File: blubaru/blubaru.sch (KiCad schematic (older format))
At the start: 24 parts, among them J1 TPA6112, J2 RN52_BREAKOUT

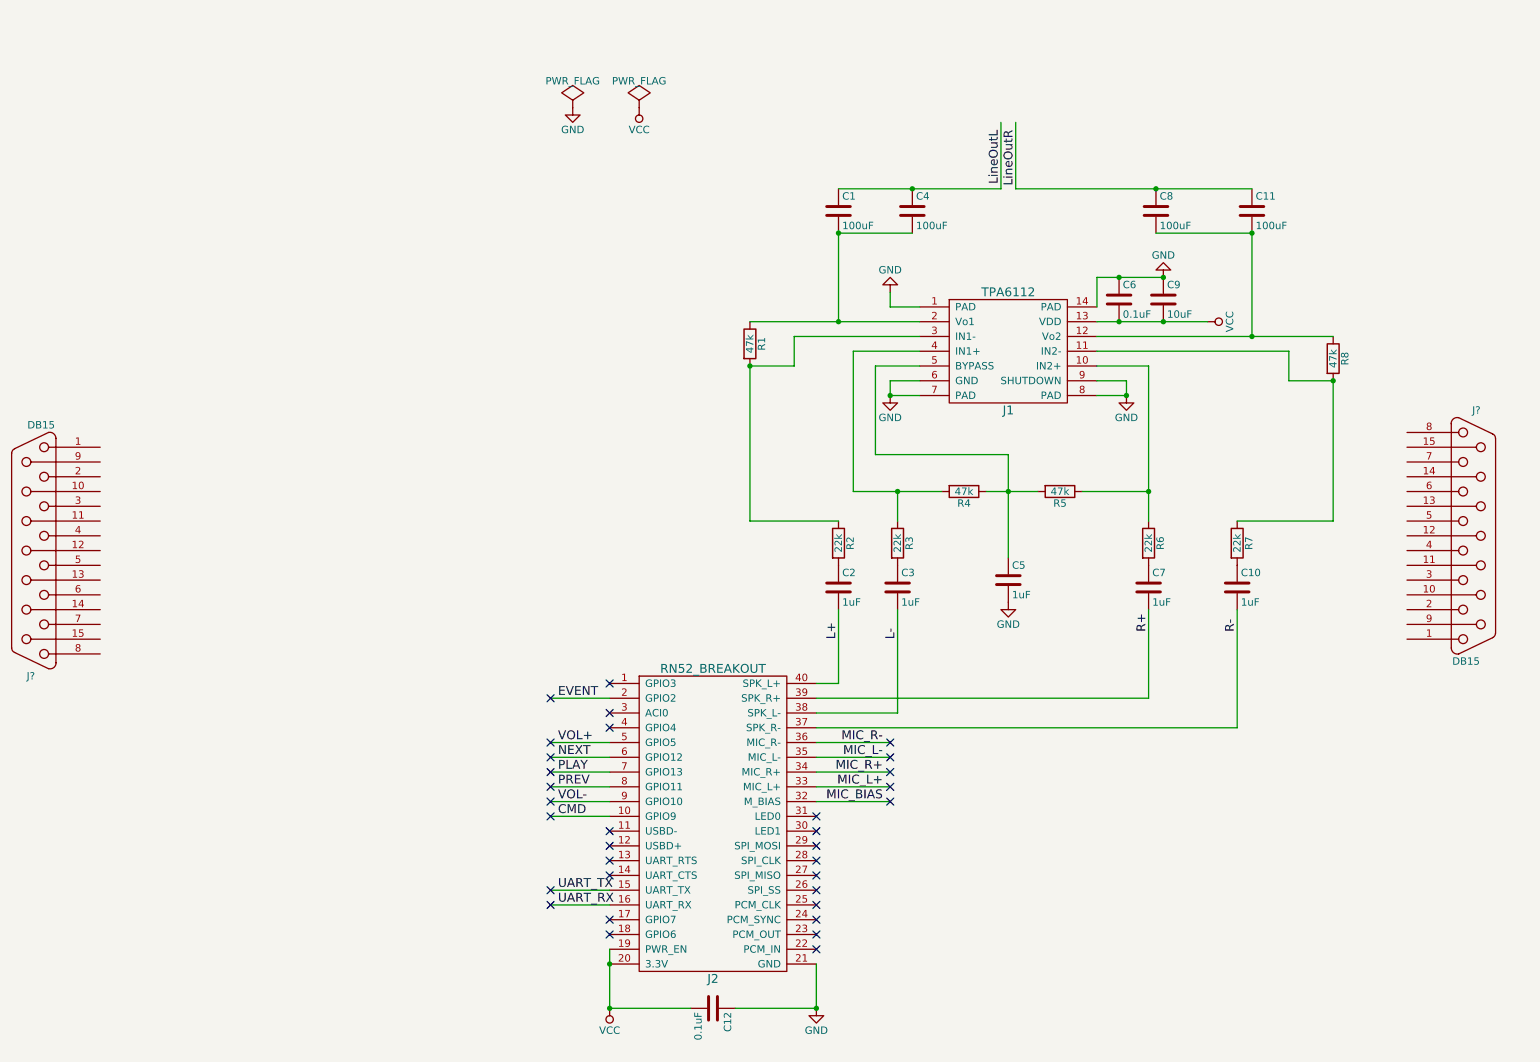
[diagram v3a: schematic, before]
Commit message: Add ProMicro board and DB15 labels
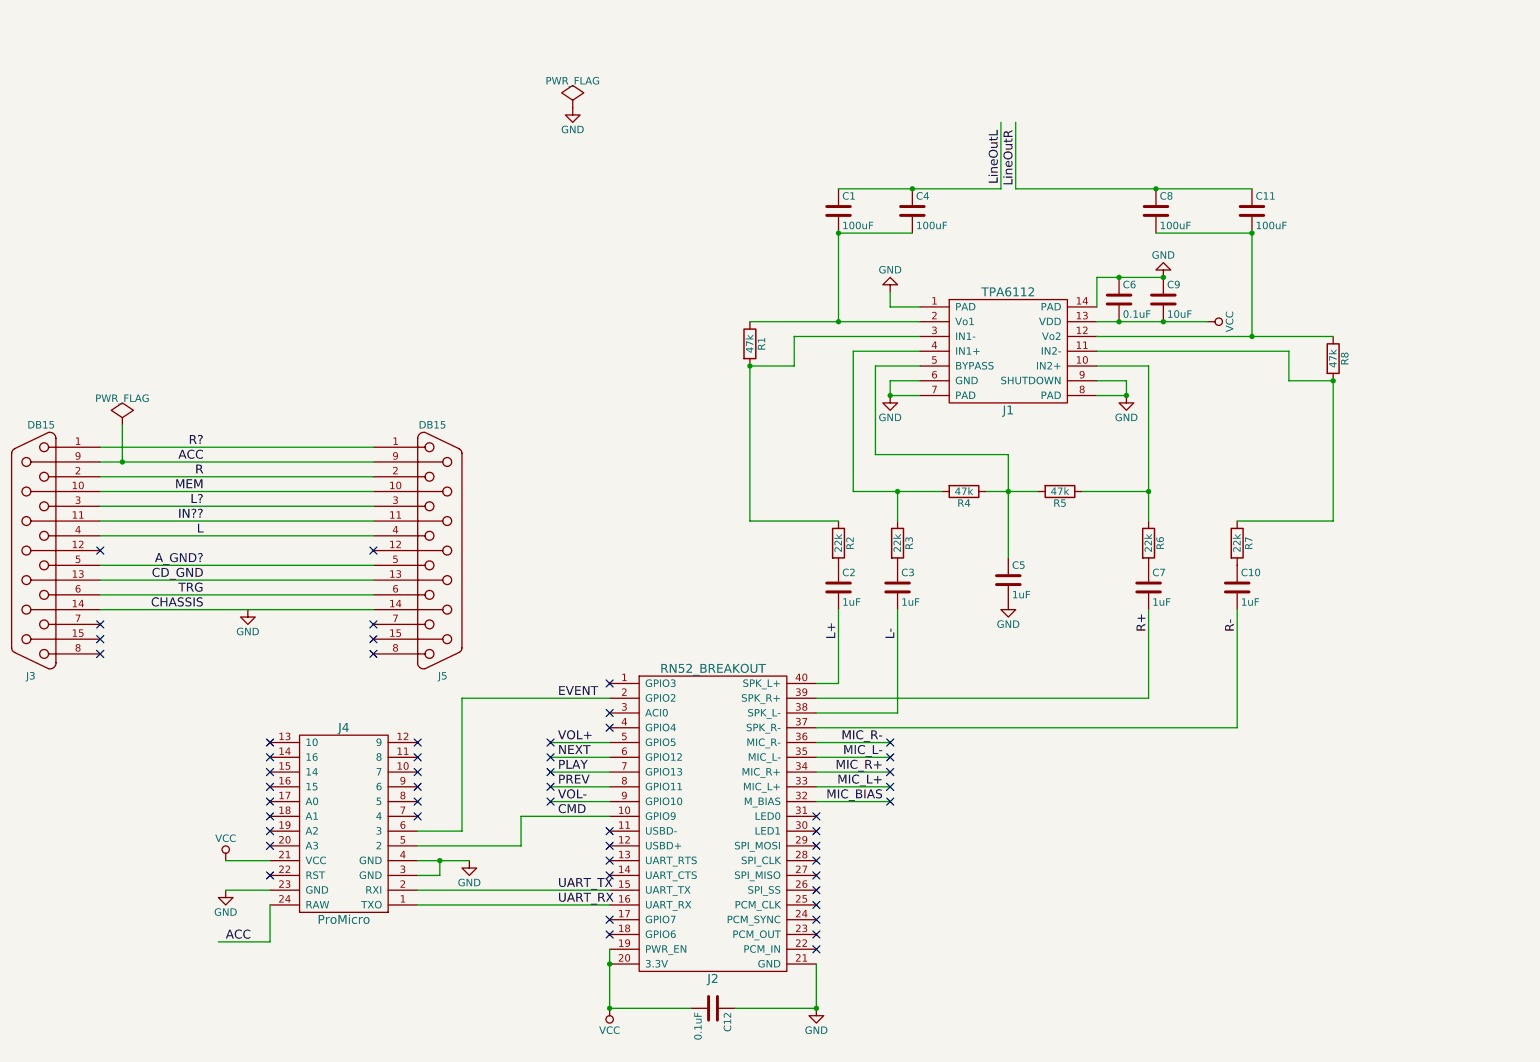
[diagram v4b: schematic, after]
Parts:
- added J4: ProMicro, symbol ProMicro
- gave numbers to parts that had none: 2
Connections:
- net labels added: ACC, A_GND?, CD_GND, CHASSIS, IN??, L, L?, MEM, R, R?, TRG
- wire segments 69 -> 92
- no-connect marks 33 -> 52
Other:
- moved on the sheet: J5

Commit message: Add a microphone jack
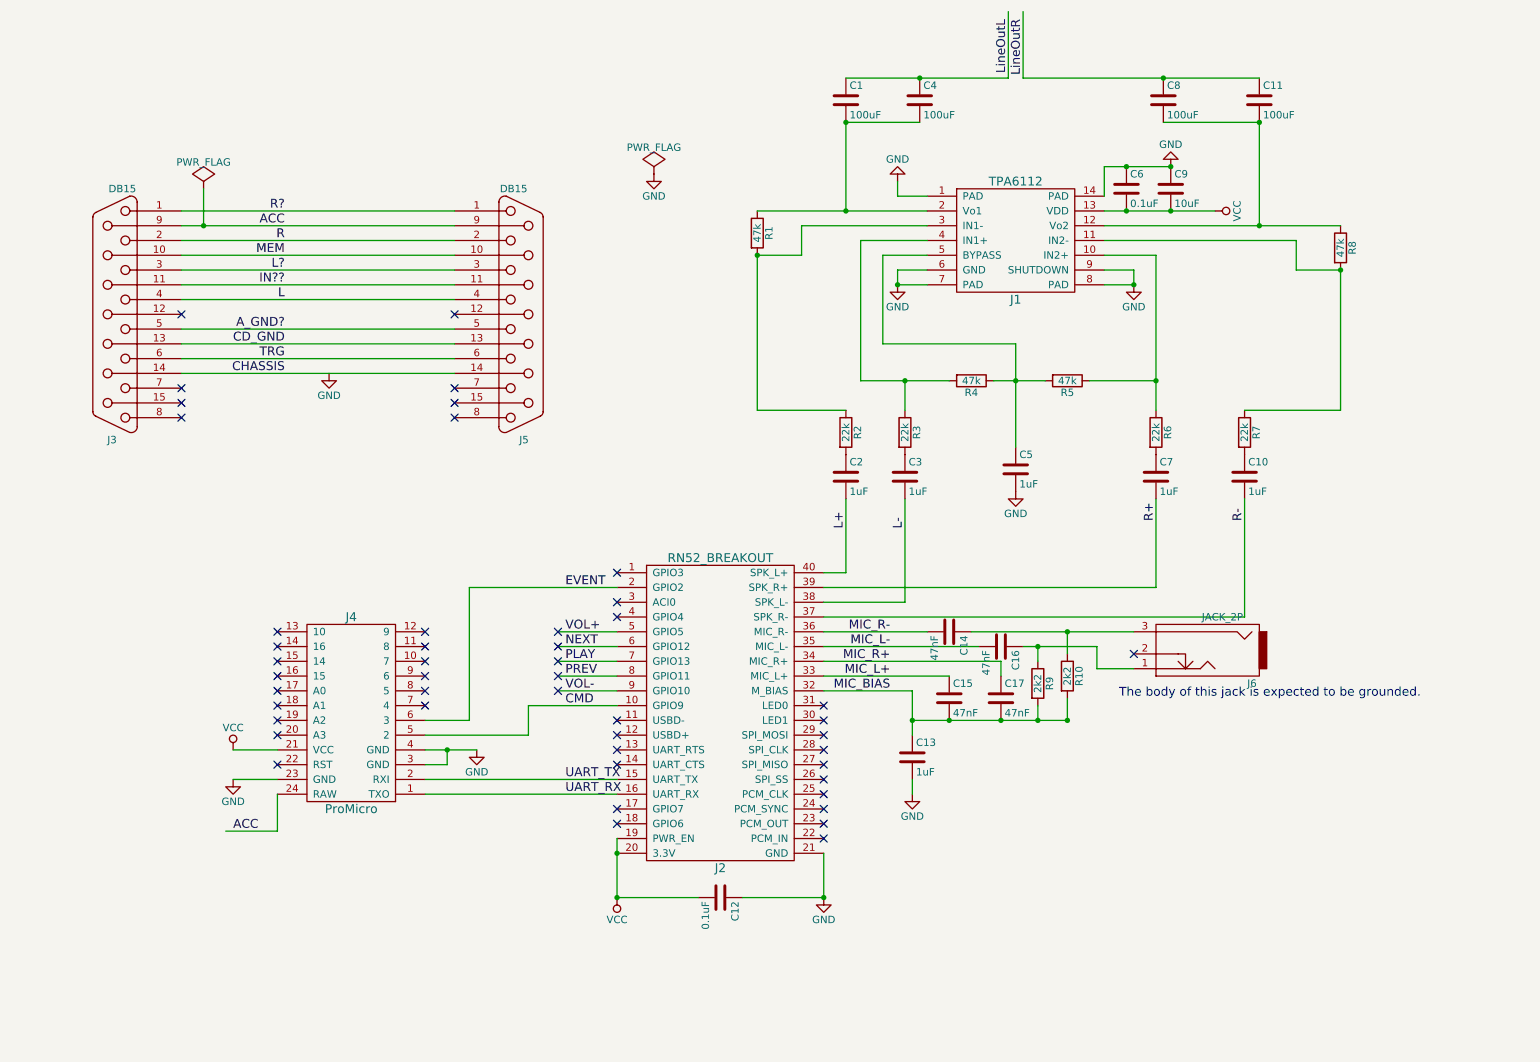
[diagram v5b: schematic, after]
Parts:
- added C13: 1uF, symbol C
- added C14, C15, C16, C17: 47nF, symbol C
- added J6: JACK_2P, symbol JACK_2P
- added R10, R9: 2k2, symbol R
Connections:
- wire segments 92 -> 104
- no-connect marks 52 -> 48
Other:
- note added: "The body of this jack is expected to be grounded."
- moved on the sheet: C1, C10, C11, C12, C2, C3, C4, C5, C6, C7, C8, C9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

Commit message: Add a mic jack and a header for buttons.
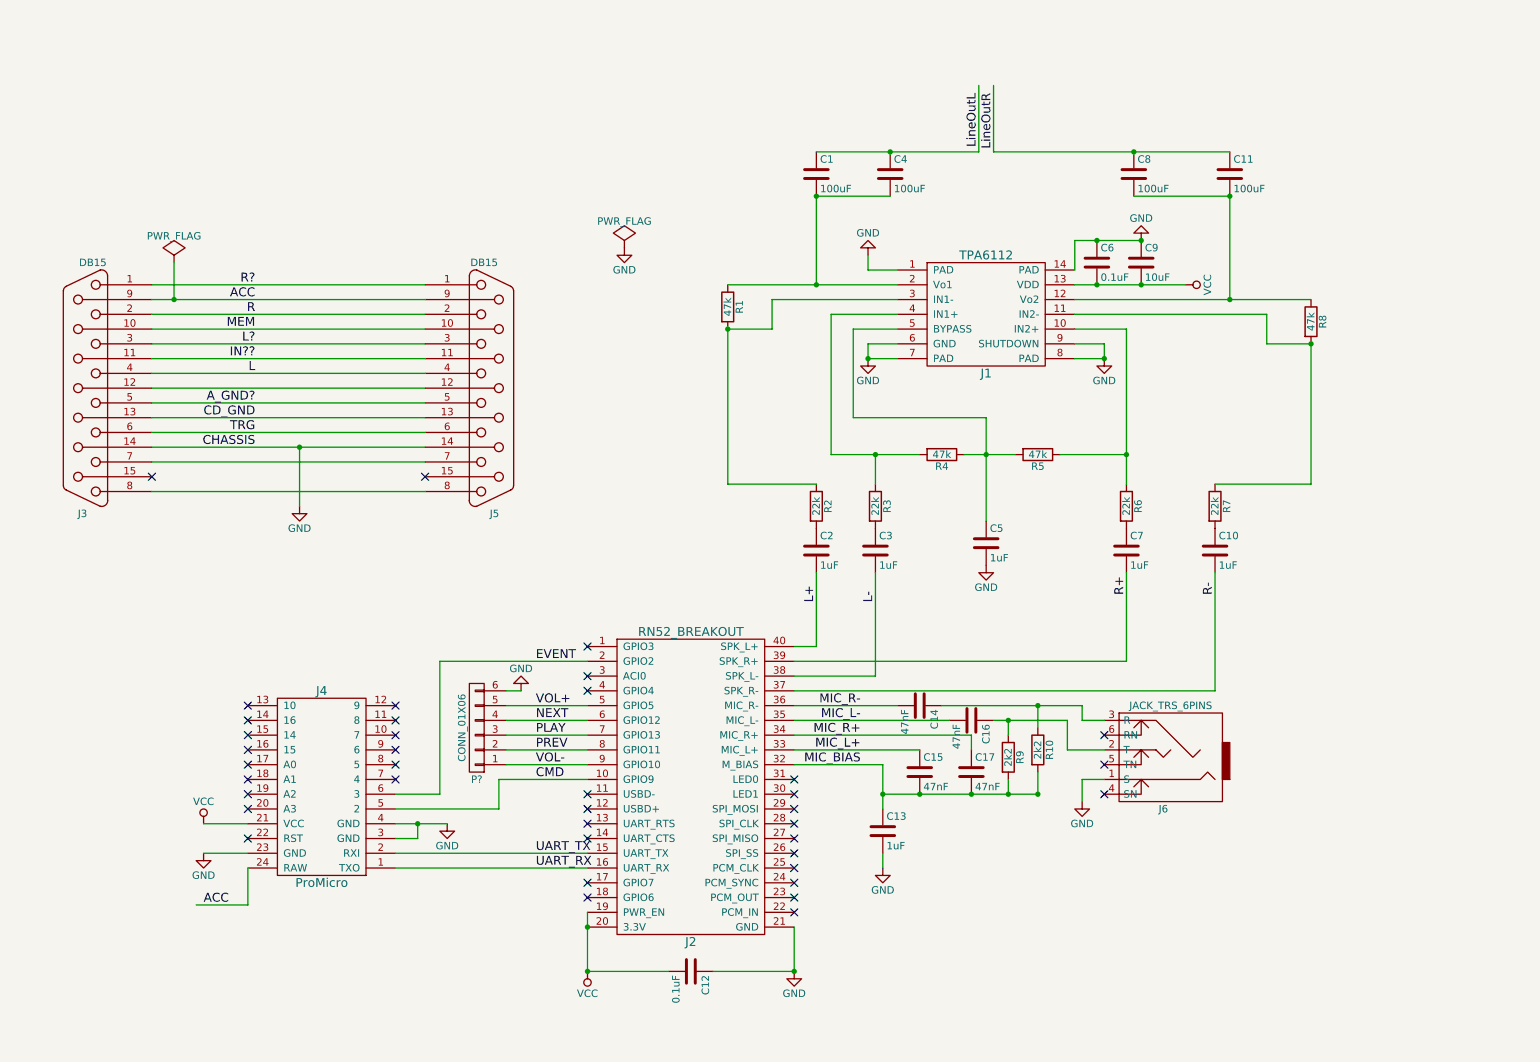
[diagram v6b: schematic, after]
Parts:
- removed J6: JACK_2P, symbol JACK_2P
- added J6: JACK_TRS_6PINS, symbol JACK_TRS_6PINS
- added P?: CONN_01X06, symbol CONN_01X06
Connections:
- net CHASSIS is gone; now on net GND: J3.14 (P14), J5.14 (P14)
- net GND: now also J6.1 (S), P?.6 (P6)
- net NEXT: now also P?.4 (P4)
- net PLAY: now also P?.3 (P3)
- net PREV: now also P?.2 (P2)
- net VOL+: now also P?.5 (P5)
- net VOL-: now also P?.1 (P1)
- net at J5.12 (P12): now also J3.12 (P12)
- net at J5.7: now also J3.7
- net at J5.8: now also J3.8
- net at C16.1, R9.1: now also J6.2 (T)
- net at C14.1, R10.1: now also J6.3 (R)
- no-connect marks 48 -> 39
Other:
- note removed: "The body of this jack is expected to be grounded."
- moved on the sheet: C1, C10, C11, C12, C13, C14, C15, C16, C17, C2, C3, C4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

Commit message: Make a virtual audio switch part.
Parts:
- added J7: AUDIO_SWITCH, symbol AUDIO_SWITCH
- gave numbers to parts that had none: 1
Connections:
- net labels added: BT_TRG, L_CD, L_STEREO, R_CD, R_STEREO, TRG_CD, TRG_STEREO
- net labels removed: L, R, TRG
- wire segments 113 -> 132
- no-connect marks 39 -> 38
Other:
- moved on the sheet: J3, J5

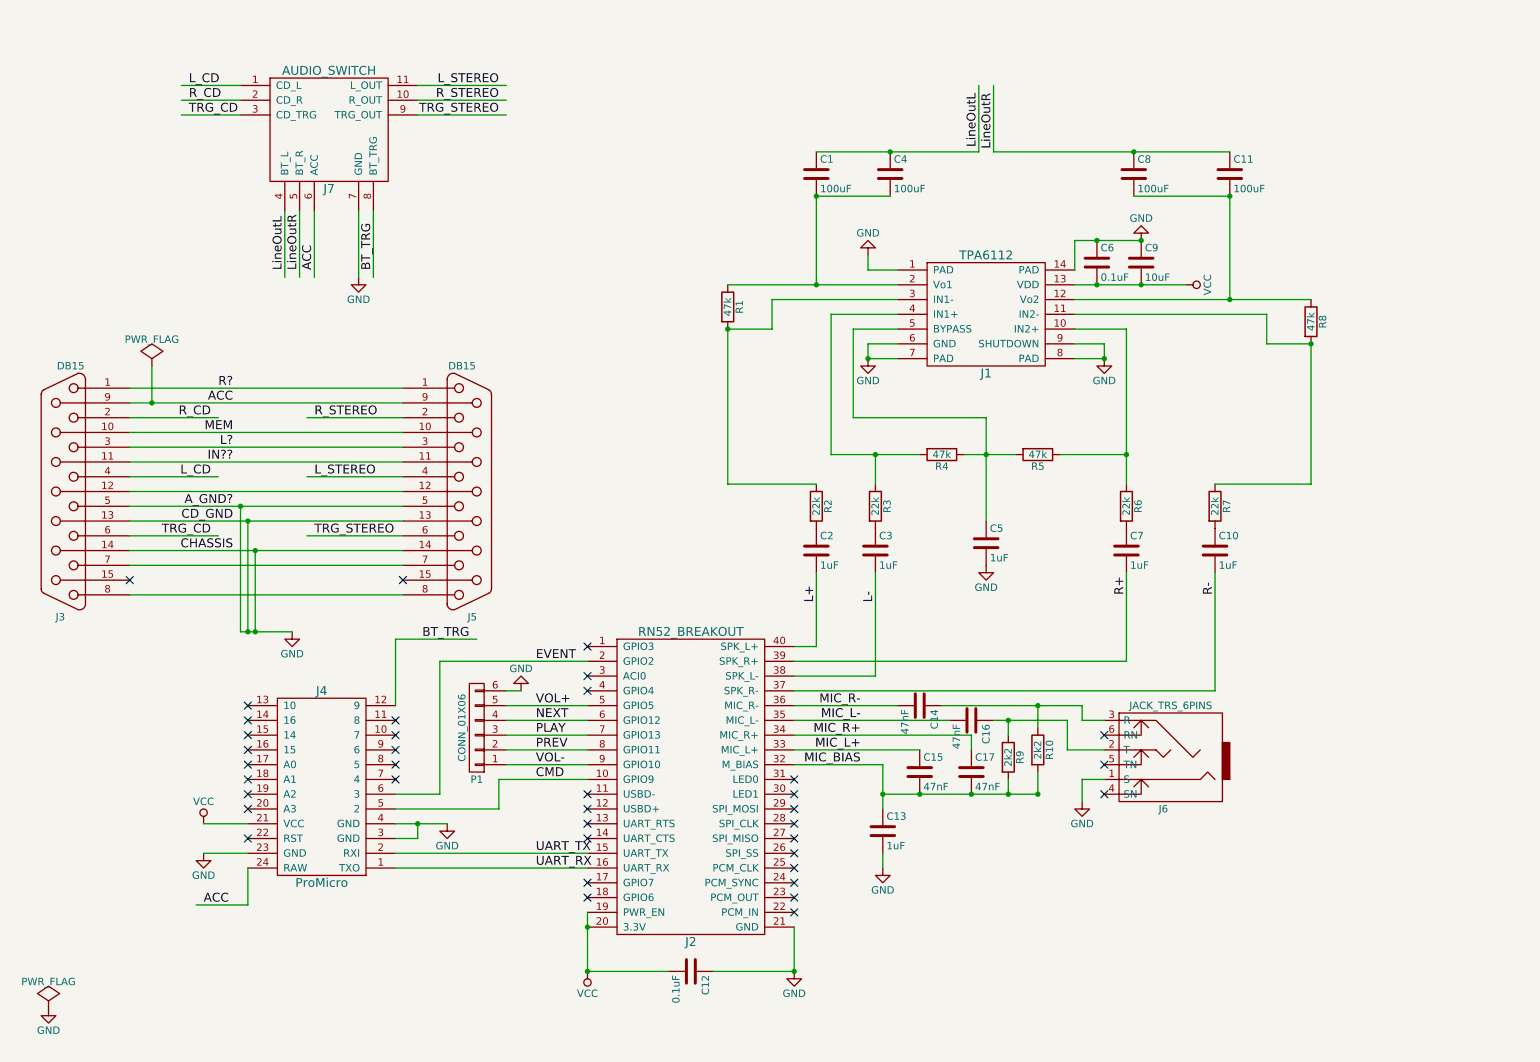
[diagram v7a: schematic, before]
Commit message: Break up into hierarchical sheets.
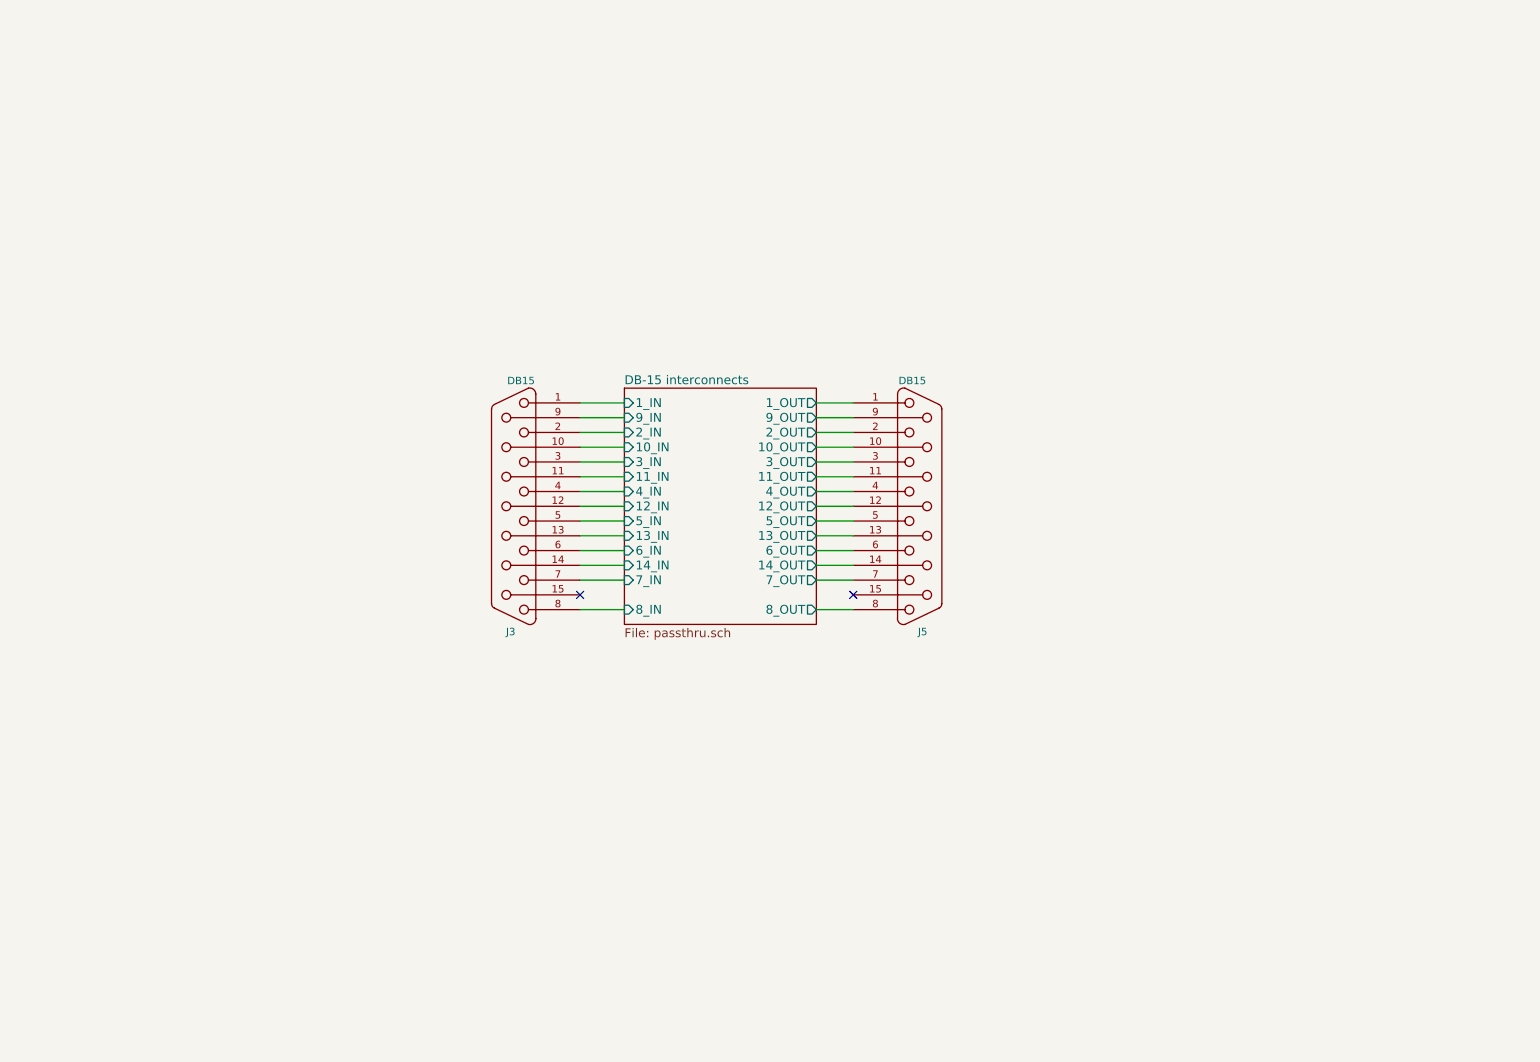
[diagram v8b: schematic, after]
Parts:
- removed C1, C11, C4, C8: 100uF, symbol C
- removed C10, C13, C2, C3, C5, C7: 1uF, symbol C
- removed C12, C6: 0.1uF, symbol C
- removed C14, C15, C16, C17: 47nF, symbol C
- removed C9: 10uF, symbol C
- removed J1: TPA6112, symbol TPA6112
- removed J2: RN52_BREAKOUT, symbol RN52_BREAKOUT
- removed J4: ProMicro, symbol ProMicro
- removed J6: JACK_TRS_6PINS, symbol JACK_TRS_6PINS
- removed J7: AUDIO_SWITCH, symbol AUDIO_SWITCH
- removed P1: CONN_01X06, symbol CONN_01X06
- removed R1, R4, R5, R8: 47k, symbol R
- removed R10, R9: 2k2, symbol R
- removed R2, R3, R6, R7: 22k, symbol R
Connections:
- net labels removed: ACC, A_GND?, BT_TRG, CD_GND, CHASSIS, CMD, EVENT, GND, IN??, L+, L-, L?, L_CD, L_STEREO, LineOutL, LineOutR, MEM, MIC_BIAS, MIC_L+, MIC_L-, MIC_R+, MIC_R-, NEXT, PLAY, PREV, R+, R-, R?, R_CD, R_STEREO, TRG_CD, TRG_STEREO, UART_RX, UART_TX, VCC, VOL+, VOL-
- wire segments 132 -> 28
- no-connect marks 38 -> 2
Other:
- moved on the sheet: J3, J5
